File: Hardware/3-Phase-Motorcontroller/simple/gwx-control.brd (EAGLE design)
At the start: 46 x 31 mm, 11 parts, among them IC1 74LS02N

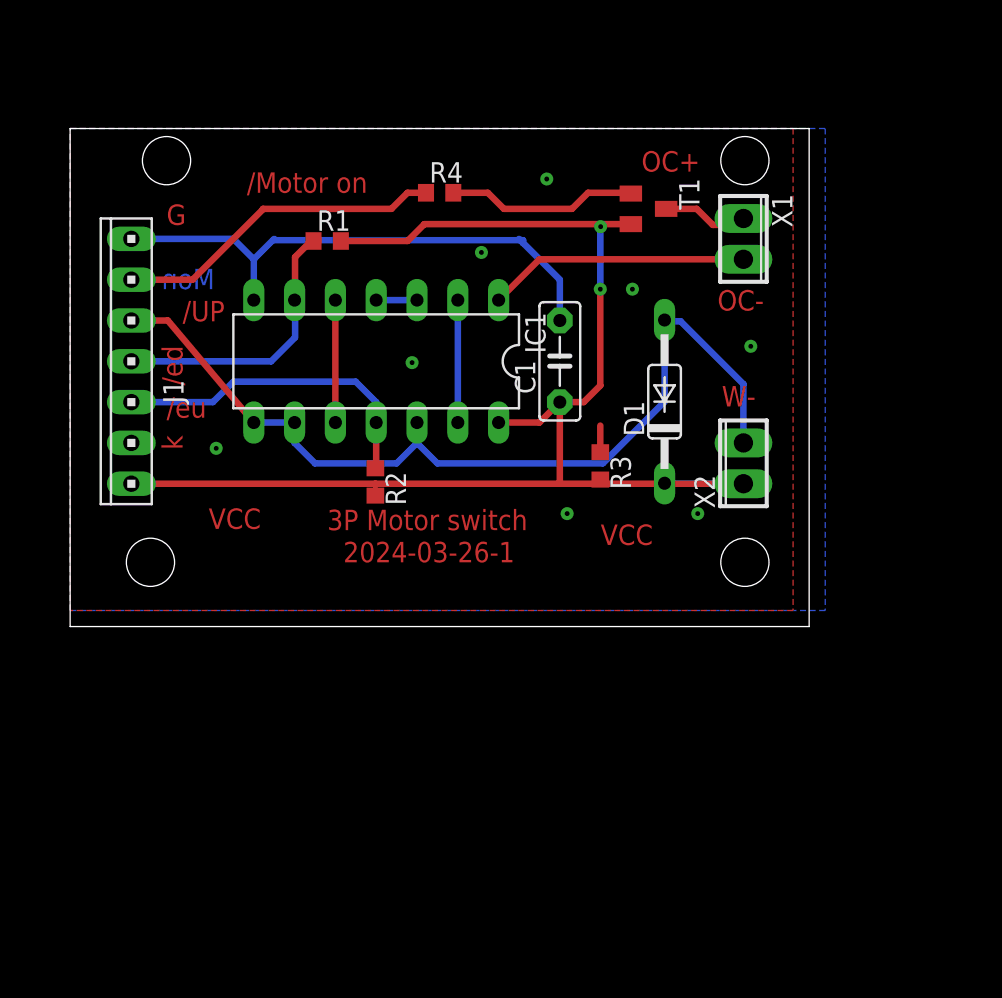
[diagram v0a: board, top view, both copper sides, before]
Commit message: added power switch protection
motor will stop for a few seconds, if direction changes
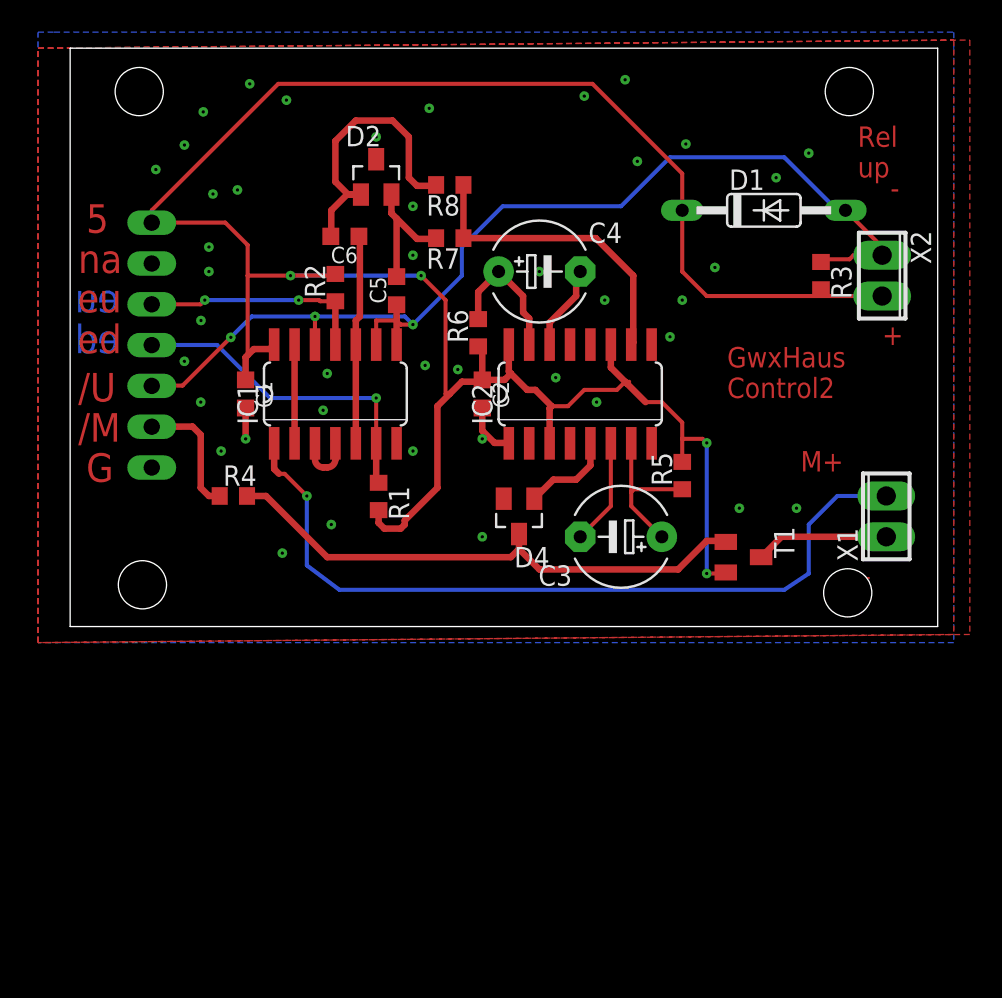
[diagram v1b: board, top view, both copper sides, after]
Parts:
- added C2: 100n, rcl:C0603K
- added C3, C4: (no value), rcl:E5-6
- added C5, C6: (no value), rcl:C0603K
- added D2: BAS40-06, diode:SOT23
- added D4: BAS40, diode:SOT23
- added IC2: 74LS123D, 74xx-eu:SO16
- added R5, R6, R7, R8: (no value), rcl:R0603
- C1: device capacitor-wima:C5B2.5 -> rcl:C0603K
- IC1: value 74LS02N -> 74LS02D; device 74xx-eu:DIL14 -> 74xx-eu:SO14
- R4: value 4k7 -> 10k
- moved R4 22.8 mm to (10.2, 8.13)
- moved T1 22.5 mm to (41.9, 4.32)
- moved C1 19.7 mm to (10.9, 14.5), turned to 270 degrees
- moved X1 19.4 mm to (50.8, 6.86), turned to 90 degrees
- moved R3 18.1 mm to (46.7, 21.8)
- moved R1 16.2 mm to (19.2, 8.10), turned to 270 degrees
- moved X2 14.5 mm to (50.5, 21.8), turned to 270 degrees
- moved D1 13.4 mm to (43.2, 25.9), turned to 0 degrees
- moved R2 12.4 mm to (16.5, 21.1), turned to 90 degrees
- moved IC1 3.25 mm to (16.5, 14.5), turned to 0 degrees
- moved J1 1.62 mm to (5.08, 17.5), flipped to the bottom, turned to 270 degrees
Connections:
- new net /Q: IC2.12
- new net FORCE_OFF: D4.1, IC2.5
- new net N$10: D4.3, R4.2, T1.B
- new net N$2: C3.-, IC2.6
- new net N$4: C5.2, D2.2, R7.2
- new net N$7: C6.2, D2.1, R8.2
- new net N$8: IC2.10, R7.1, R8.1
- new net N$9: C4.-, IC2.14
- new net UP: C6.1, IC1.10, IC1.5
- net /UP: now also C5.1, X2.1; no longer X2.2
- net GND: now also C2.2, D2.3, IC2.1, IC2.2, IC2.8, IC2.9
- net N$1: now also C3.+, IC2.7, R5.1; no longer IC1.10, IC1.5
- net N$3: now also C4.+, IC2.15, R6.2; no longer R4.2, T1.B
- net VCC: now also C2.1, IC2.11, IC2.16, IC2.3, R5.2, R6.1, X2.2; no longer X2.1
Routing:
- net VCC: track 86.2 -> 149.5 mm, vias 2 -> 4
- net N$10: track 0.00 -> 33.8 mm
- net /OK: track 16.3 -> 49.3 mm, vias 0 -> 1
- net GND: track 34.3 -> 5.05 mm, vias 8 -> 41
- net N$8: track 0.00 -> 19.2 mm
- net N$7: track 0.00 -> 18.3 mm
- net UP: track 0.00 -> 13.0 mm
- net /MOTOR_ON: track 20.6 -> 7.95 mm
- net /UP: track 58.8 -> 67.8 mm, vias 0 -> 3
- net N$4: track 1.00 -> 8.24 mm
- net N$2: track 0.00 -> 6.61 mm
- net /END_UP: track 20.4 -> 14.3 mm, vias 0 -> 2
- net FORCE_OFF: track 0.00 -> 5.73 mm
- net N$9: track 0.00 -> 5.34 mm
- net /END_DOWN: track 17.4 -> 20.7 mm, vias 0 -> 1
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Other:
- board size 46 x 31 mm -> 54 x 36 mm
- board text added: "+"
- board text added: "-"
- board text added: "/M"
- board text added: "/U"
- board text added: "5"
- board text added: "GwxHaus Control2"
- board text added: "M+"
- board text added: "Rel up"
- board text added: "ed"
- board text added: "eu"
- board text added: "na"
- board text removed: "/Motor on"
- board text removed: "/UP"
- board text removed: "/ed"
- board text removed: "/eu"
- board text removed: "2024-03-26-1"
- board text removed: "3P Motor switch"
- board text removed: "Mon"
- board text removed: "OC+"
- board text removed: "OC-"
- board text removed: "VCC"
- board text removed: "W-"
- board text removed: "k"

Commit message: Trigger fixed
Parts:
- removed D2: BAS40-06, diode:SOT23
- added D3: BAT54C, diode:SOT23
- added R9: 47k, rcl:R0603
- C3: value (none) -> 47µ
- R5, R7, R8: value (none) -> 47k
- moved R8 7.55 mm to (16.6, 24.8), turned to 270 degrees
- moved C6 3.51 mm to (18.3, 21.0), turned to 90 degrees
- moved R7 1.72 mm to (22.0, 24.6), turned to 90 degrees
- moved C5 0.13 mm to (20.3, 21.0)
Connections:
- net GND: now also R7.2, R8.1, R9.2; no longer D2.3
- net N$4: now also D3.2, R7.1; no longer D2.2, R7.2
- net N$7: now also D3.1; no longer D2.1
- net N$8: now also D3.3, R9.1; no longer R7.1, R8.1
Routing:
- net N$7: track 18.3 -> 4.09 mm
- net VCC: track 149.5 -> 139.4 mm
- net N$8: track 19.2 -> 23.5 mm
- net N$4: track 8.24 -> 3.98 mm
- net UP: track 13.0 -> 8.94 mm
- net GND: vias 41 -> 44

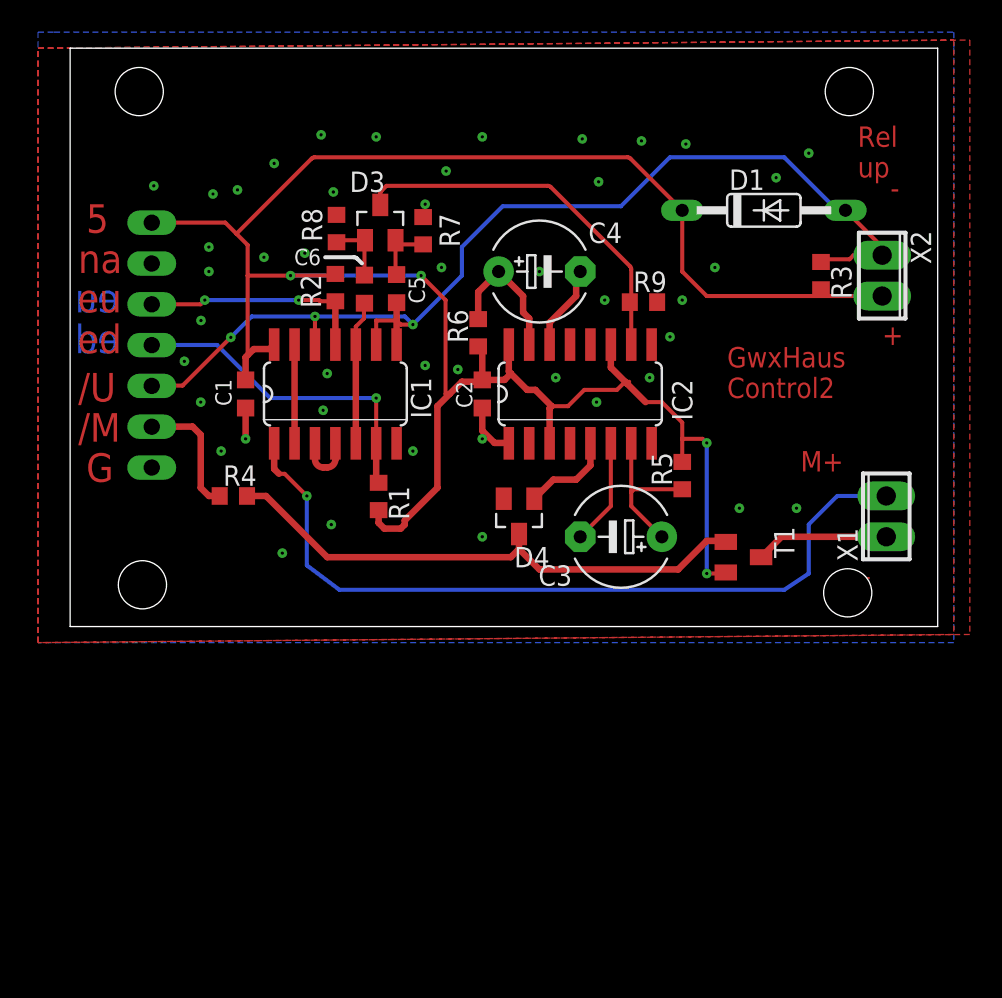
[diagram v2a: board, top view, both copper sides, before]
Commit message: force motor off is now more relyable
changed from pull down the base of t1 to active switch a 2n T in series
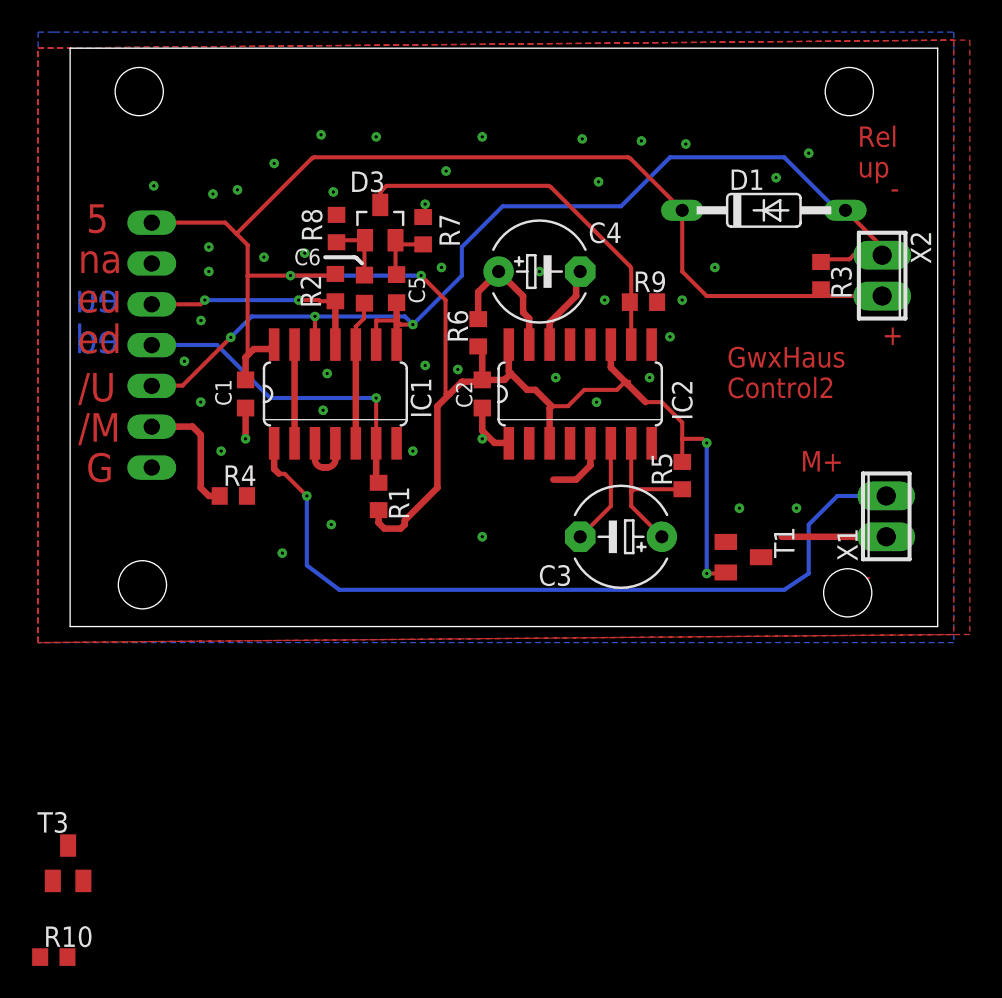
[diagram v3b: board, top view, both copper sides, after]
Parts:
- removed D4: BAS40, diode:SOT23
- added R10: 10k, resistor:R0603
- added T3: (no value), transistor:SOT23-BEC
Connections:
- removed net /Q: IC2.12
- removed net FORCE_OFF: D4.1, IC2.5
- new net /MOTOR_OK: IC2.12, R10.1
- new net N$11: R4.2, T1.B
- new net N$12: T1.C, T3.E
- new net Q1: IC2.5
- net MOTOR_ON+: now also T3.C; no longer T1.C
- net N$10: now also R10.2, T3.B; no longer D4.3, R4.2, T1.B
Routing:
- net N$10: track 33.8 -> 0.00 mm
- net FORCE_OFF: track 5.73 -> 0.00 mm
- net Q1: track 0.00 -> 4.05 mm
- net MOTOR_ON+: track 8.32 -> 6.52 mm
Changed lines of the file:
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@@
 <attribute name="VALUE" x="14.676" y="25.408" size="1.27" layer="27" rot="R270"/>
-</element>
-<element name="D4" library="diode" package="SOT23" value="BAS40" x="27.94" y="6.858" smashed="yes" rot="R180">
-<attribute name="NAME" x="29.845" y="4.953" size="1.27" layer="25" rot="R180"/>
-<attribute name="VALUE" x="29.845" y="10.033" size="1.27" layer="27" rot="R180"/>
 </element>
 <element name="D3" library="diode" package="SOT23" value="BAT54C" x="19.304" y="25.146"/>
@@
 </element>
 <element name="R9" library="rcl" package="R0603" value="47k" x="35.687" y="20.193"/>
+<element name="T3" library="transistor" package="SOT23-BEC" value="" x="-0.127" y="-14.732"/>
+<element name="R10" library="resistor" package="R0603" value="10k" x="-1.016" y="-20.574"/>
 </elements>
 <signals>
@@
 <signal name="MOTOR_ON+">
 <contactref element="X1" pad="1"/>
-<contactref element="T1" pad="C"/>
-<wire x1="43.01" y1="4.318" x2="44.28" y2="5.588" width="0.4064" layer="1"/>
 <wire x1="44.28" y1="5.588" x2="50.8" y2="5.588" width="0.4064" layer="1"/>
+<contactref element="T3" pad="C"/>
+<wire x1="-0.127" y1="-13.632" x2="44.28" y2="5.588" width="0" layer="19" extent="1-1"/>
 </signal>
 <signal name="N$1">
@@
 <wire x1="34.837" y1="20.193" x2="34.925" y2="20.193" width="0.254" layer="1"/>
 </signal>
-<signal name="N$10">
-<contactref element="T1" pad="B"/>
-<contactref element="R4" pad="2"/>
-<contactref element="D4" pad="3"/>
-<wire x1="27.94" y1="4.826" x2="29.21" y2="3.556" width="0.4064" layer="1"/>
-<wire x1="29.21" y1="3.556" x2="37.846" y2="3.556" width="0.4064" layer="1"/>
-<wire x1="37.846" y1="3.556" x2="39.624" y2="5.334" width="0.4064" layer="1"/>
-<wire x1="39.624" y1="5.334" x2="40.744" y2="5.334" width="0.4064" layer="1"/>
-<wire x1="40.744" y1="5.334" x2="40.81" y2="5.268" width="0.4064" layer="1"/>
-<wire x1="27.94" y1="5.758" x2="27.94" y2="4.826" width="0.4064" layer="1"/>
-<wire x1="27.94" y1="4.826" x2="27.432" y2="4.318" width="0.4064" layer="1"/>
-<wire x1="27.432" y1="4.318" x2="16.002" y2="4.318" width="0.4064" layer="1"/>
-<wire x1="16.002" y1="4.318" x2="12.192" y2="8.128" width="0.4064" layer="1"/>
-<wire x1="12.192" y1="8.128" x2="11.01" y2="8.128" width="0.4064" layer="1"/>
-</signal>
-<signal name="/Q">
-<contactref element="IC2" pad="12"/>
-</signal>
 <signal name="N$3">
 <contactref element="C4" pad="+"/>
@@
 <wire x1="31.496" y1="21.844" x2="31.75" y2="22.098" width="0.4064" layer="1"/>
 </signal>
-<signal name="FORCE_OFF">
+<signal name="N$13">
+<via x="29.21" y="22.098" extent="1-16" drill="0.2" diameter="0.254"/>
+</signal>
+<signal name="N$11">
+<contactref element="T1" pad="B"/>
+<contactref element="R4" pad="2"/>
+<wire x1="11.01" y1="8.128" x2="40.81" y2="5.268" width="0" layer="19" extent="1-1"/>
+</signal>
+<signal name="N$12">
+<contactref element="T1" pad="C"/>
+<contactref element="T3" pad="E"/>
+<wire x1="0.823" y1="-15.832" x2="43.01" y2="4.318" width="0" layer="19" extent="1-1"/>
+</signal>
+<signal name="N$10">
+<contactref element="R10" pad="2"/>
+<contactref element="T3" pad="B"/>
+<wire x1="-1.077" y1="-15.832" x2="-0.166" y2="-20.574" width="0" layer="19" extent="1-1"/>
+</signal>
+<signal name="/MOTOR_OK">
+<contactref element="R10" pad="1"/>
+<contactref element="IC2" pad="12"/>
+<wire x1="-1.866" y1="-20.574" x2="32.385" y2="17.5514" width="0" layer="19" extent="1-1"/>
+</signal>
+<signal name="Q1">
 <contactref element="IC2" pad="5"/>
-<contactref element="D4" pad="1"/>
 <wire x1="32.385" y1="11.4046" x2="32.385" y2="10.033" width="0.4064" layer="1"/>
 <wire x1="32.385" y1="10.033" x2="31.496" y2="9.144" width="0.4064" layer="1"/>
 <wire x1="31.496" y1="9.144" x2="30.076" y2="9.144" width="0.4064" layer="1"/>
-<wire x1="30.076" y1="9.144" x2="28.89" y2="7.958" width="0.4064" layer="1"/>
-</signal>
-<signal name="N$13">
-<via x="29.21" y="22.098" extent="1-16" drill="0.2" diameter="0.254"/>
 </signal>
 </signals>

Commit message: Changed Motor force off to non inverted mono flop output
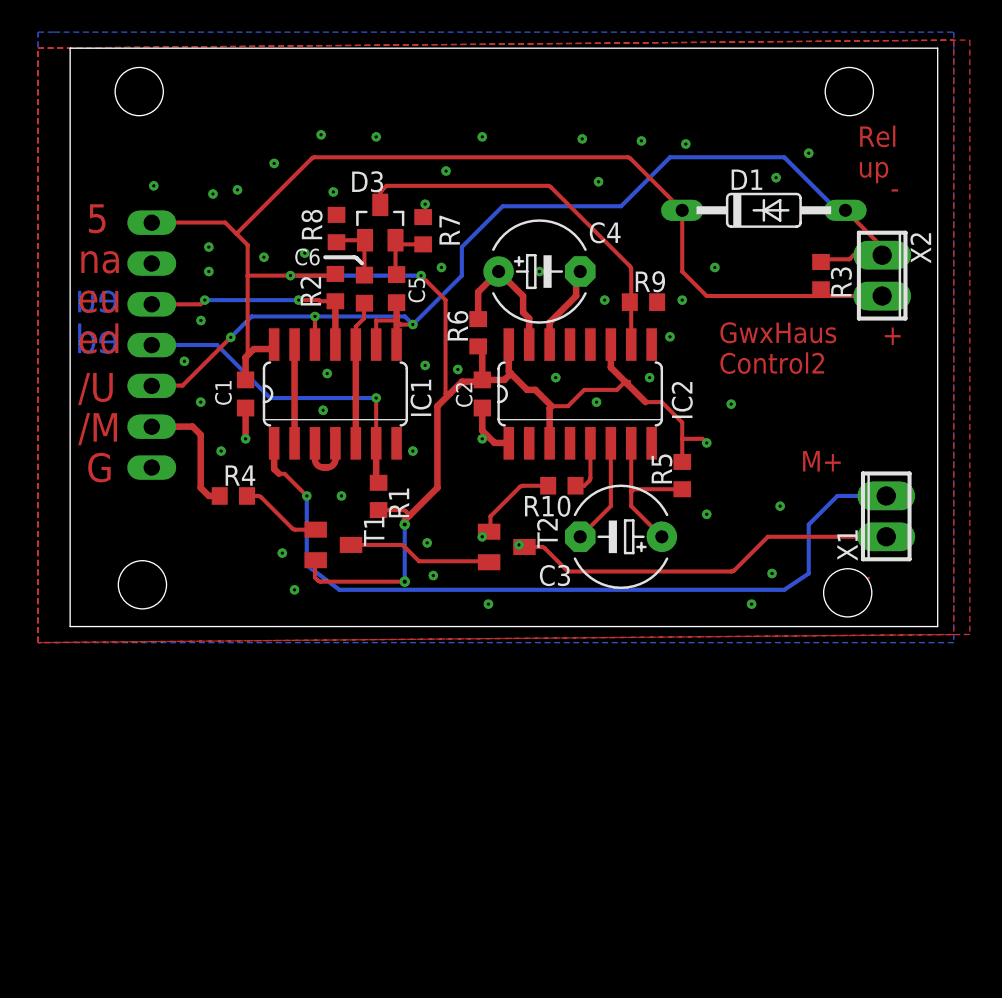
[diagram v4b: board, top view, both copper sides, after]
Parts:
- removed T3: (no value), transistor:SOT23-BEC
- added T2: BC850, transistor:SOT23-BEC
- C5, C6: value (none) -> 100p
- T1: value (none) -> BC850
- moved R10 43.1 mm to (30.6, 8.76), turned to 180 degrees
- moved T1 25.5 mm to (16.4, 5.08)
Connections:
- removed net Q1: IC2.5
- new net /Q: IC2.12
- net /MOTOR_OK: now also IC2.5; no longer IC2.12
- net MOTOR_ON+: now also T2.C; no longer T3.C
- net N$10: now also T2.B; no longer T3.B
- net N$12: now also T2.E; no longer T3.E
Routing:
- net MOTOR_ON+: track 6.52 -> 24.0 mm
- net N$12: track 0.00 -> 9.01 mm
- net N$10: track 0.00 -> 5.34 mm
- net N$11: track 0.00 -> 5.11 mm
- net Q1: track 4.05 -> 0.00 mm
- net /MOTOR_OK: track 0.00 -> 3.33 mm
- net VCC: track 139.4 -> 139.8 mm, vias 4 -> 5
- net GND: vias 44 -> 52
